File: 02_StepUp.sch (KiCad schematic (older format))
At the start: 31 parts, among them J301 Conn_02x04_Odd_Even, J302 Conn_02x04_Odd_Even, Q201 VS6412AE, U202 StepUp, U203 TPS40210

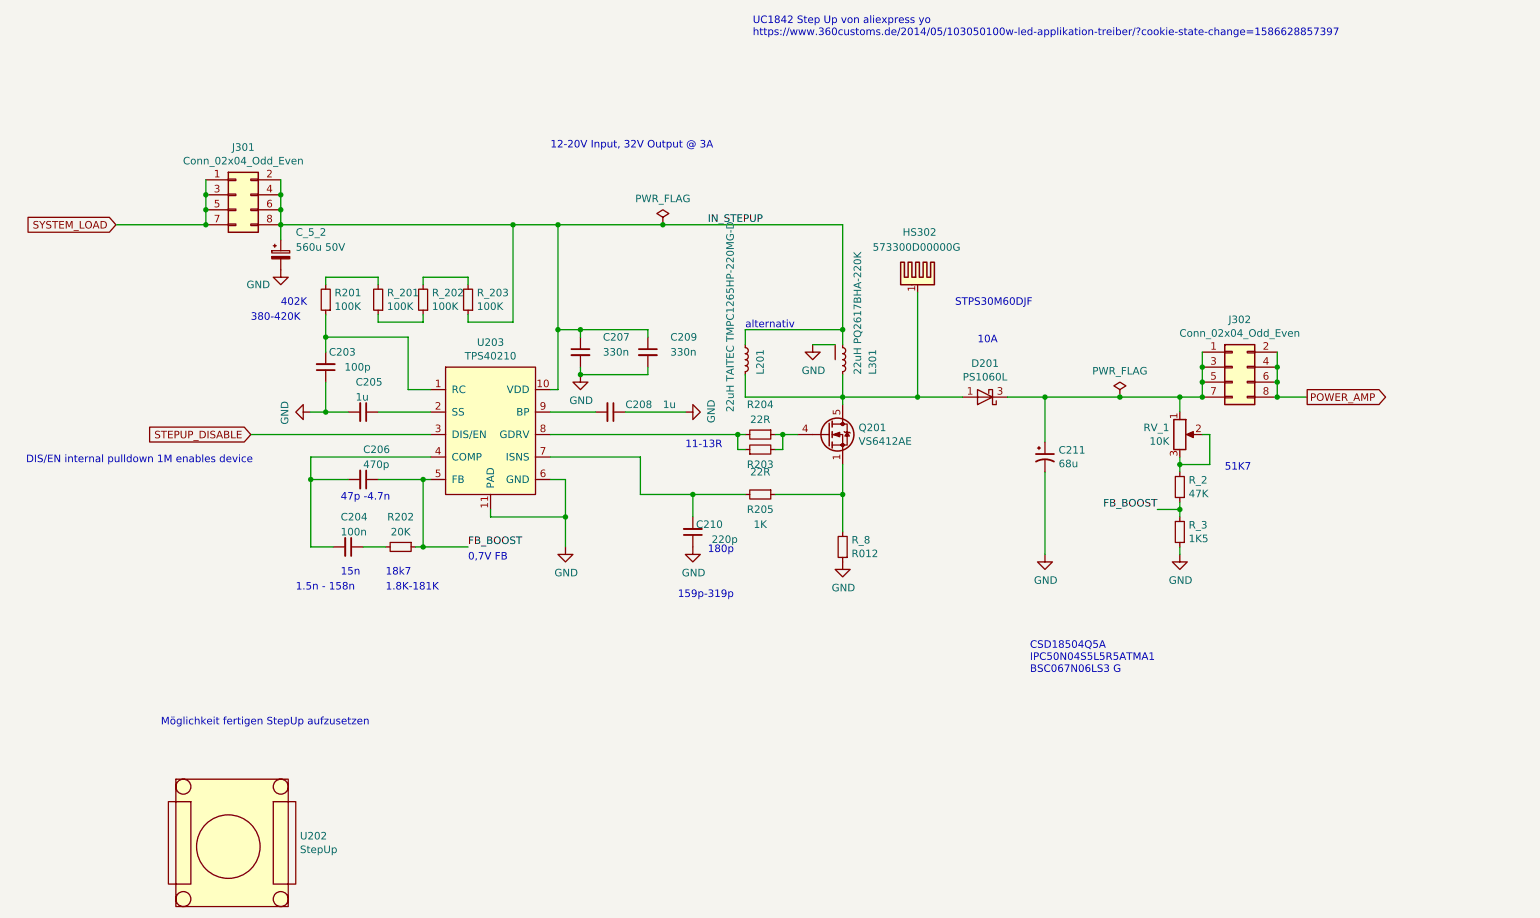
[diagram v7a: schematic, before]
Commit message: Platine in X um 25mm verkürzt
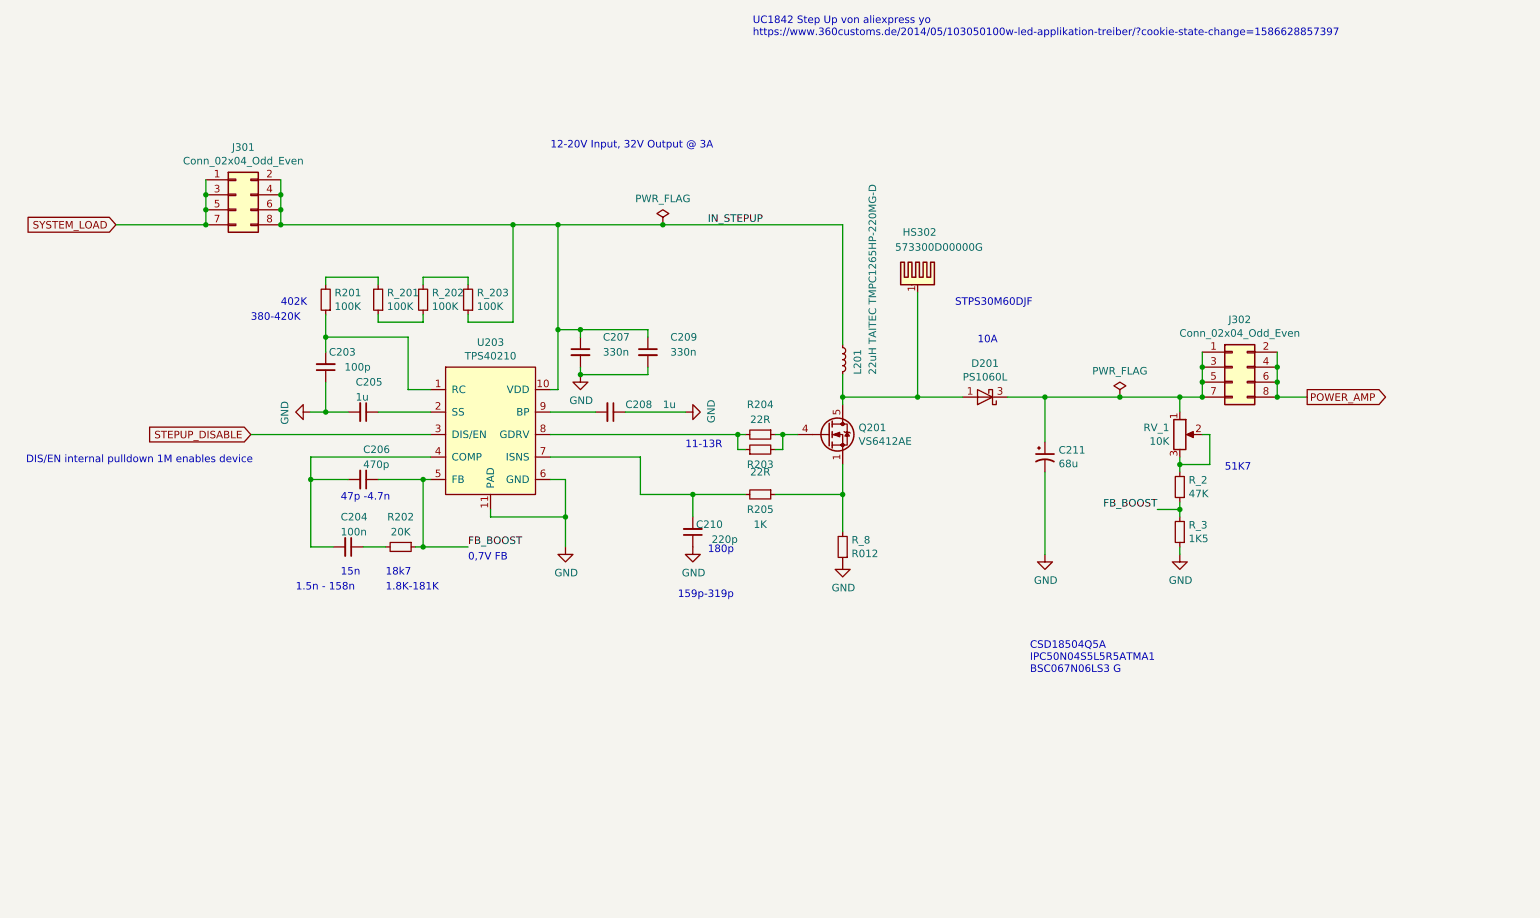
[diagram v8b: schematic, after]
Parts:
- removed C_5_2: 560u 50V, Capacitor_THT:CP_Radial_D12.5mm_P5.00mm, symbol Device:CP_Small
- removed L301: 22uH PQ2617BHA-220K, Inductor_SMD:PQ2617BHA-330K, symbol MukkeBox-rescue:L_Small_3-Device-MukkeBox-rescue
- removed U202: StepUp, Module:StepUpModul, symbol MukkeBox-rescue:StepUp-MySymbols-MukkeBox-rescue
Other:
- note removed: "Möglichkeit fertigen StepUp aufzusetzen"
- note removed: "alternativ"
- moved on the sheet: L201
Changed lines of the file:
@@
 Text GLabel 1850 2400 0    50   Input ~ 0
 SYSTEM_LOAD
-Wire Wire Line
-	2950 2500 2950 2400
 Text GLabel 9800 3550 2    50   Output ~ 0
 POWER_AMP
@@
 P 7200 2750
 F 0 "HS302" H 7100 3050 50  0000 L CNN
-F 1 "573300D00000G" H 6900 2950 50  0000 L CNN
+F 1 "573300D00000G" H 7050 2950 50  0000 L CNN
 F 2 "Heatsink:Heatsink_AAVID_573300D00010G_TO-263" H 7212 2700 50  0001 C CNN
 F 3 "https://www.mouser.de/datasheet/2/2/Aavid-Board-Level-Heatsinks-Catalog-2018-1507171.pdf" H 7212 2700 50  0001 C CNN
@@
 Wire Wire Line
 	8950 4000 8950 3950
-$Comp
-L Device:CP_Small C?
-U 1 1 5E9CBBA9
-P 2950 2600
-AR Path="/5E751A81/5E9CBBA9" Ref="C?"  Part="1"
-AR Path="/5E73BAE8/5E9CBBA9" Ref="C_5_2"  Part="1"
-F 0 "C_5_2" H 3050 2750 50  0000 L CNN
-F 1 "560u 50V" H 3050 2650 50  0000 L CNN
-F 2 "Capacitor_THT:CP_Radial_D12.5mm_P5.00mm" H 2950 2600 50  0001 C CNN
-F 3 "https://www.mouser.de/datasheet/2/420/United-Chemi-Con-1109128.pdf" H 2950 2600 50  0001 C CNN
-	1    2950 2600
-	1    0    0    -1
-$EndComp
 Wire Wire Line
 	2450 2400 1850 2400
@@
 	1    0    0    -1
 $EndComp
-$Comp
-L power:GND #PWR?
-U 1 1 5F07DA47
-P 2950 2700
-AR Path="/5EA6895E/5F07DA47" Ref="#PWR?"  Part="1"
-AR Path="/5E73BAE8/5F07DA47" Ref="#PWR0207"  Part="1"
-F 0 "#PWR0207" H 2950 2450 50  0001 C CNN
-F 1 "GND" H 2800 2600 50  0000 C CNN
-F 2 "" H 2950 2700 50  0001 C CNN
-F 3 "" H 2950 2700 50  0001 C CNN
-	1    2950 2700
-	1    0    0    -1
-$EndComp
 Connection ~ 8950 3550
 Wire Wire Line
@@
 Wire Wire Line
 	8950 4300 8950 4350
-$Comp
-L MukkeBox-rescue:StepUp-MySymbols-MukkeBox-rescue U202
-U 1 1 5FE6AEE3
-P 2600 6450
-F 0 "U202" H 3078 6421 50  0000 L CNN
-F 1 "StepUp" H 3078 6330 50  0000 L CNN
-F 2 "Module:StepUpModul" H 2600 6450 50  0001 C CNN
-F 3 "" H 2600 6450 50  0001 C CNN
-	1    2600 6450
-	1    0    0    -1
-$EndComp
-Text Notes 2150 5750 0    50   ~ 0
-Möglichkeit fertigen StepUp aufzusetzen
 $Comp
 L MukkeBox-rescue:TPS40210-MySymbols-MukkeBox-rescue U203
@@
 Wire Wire Line
 	5500 2400 6700 2400
-Wire Wire Line
-	6700 2400 6700 3100
 Wire Wire Line
 	4750 3500 4800 3500
@@
 	6300 3800 6400 3800
 $Comp
-L MukkeBox-rescue:L_Small_3-Device-MukkeBox-rescue L301
-U 1 1 5EDD1CAF
-P 6700 3300
-AR Path="/5EDD1CAF" Ref="L301"  Part="1"
-AR Path="/5E73BAE8/5EDD1CAF" Ref="L301"  Part="1"
-F 0 "L301" V 6900 3200 50  0000 L CNN
-F 1 "22uH PQ2617BHA-220K" V 6800 3200 50  0000 L CNN
-F 2 "Inductor_SMD:PQ2617BHA-330K" H 6700 3300 50  0001 C CNN
-F 3 "https://www.mouser.de/datasheet/2/54/bourns_PQ2617BHA_datasheet-1159314.pdf" H 6700 3300 50  0001 C CNN
-	1    6700 3300
-	1    0    0    -1
-$EndComp
-$Comp
-L power:GND #PWR0201
-U 1 1 5EDD85E2
-P 6500 3200
-F 0 "#PWR0201" H 6500 2950 50  0001 C CNN
-F 1 "GND" H 6505 3027 50  0000 C CNN
-F 2 "" H 6500 3200 50  0001 C CNN
-F 3 "" H 6500 3200 50  0001 C CNN
-	1    6500 3200
-	1    0    0    -1
-$EndComp
-Wire Wire Line
-	6650 3200 6500 3200
-$Comp
 L Device:L_Small L201
 U 1 1 5EFA9CC8
-P 6050 3300
-F 0 "L201" V 6150 3200 50  0000 L CNN
-F 1 "22uH TAITEC TMPC1265HP-220MG-D " V 5950 2950 50  0000 L CNN
-F 2 "Inductor_SMD:TAITEC TMPC1265HP-220MG-D" H 6050 3300 50  0001 C CNN
-F 3 "https://datasheet.lcsc.com/szlcsc/TAITEC-TMPC1265HP-220MG-D_C305224.pdf" H 6050 3300 50  0001 C CNN
-	1    6050 3300
-	1    0    0    -1
-$EndComp
-Wire Wire Line
-	6050 3200 6050 3100
-Wire Wire Line
-	6050 3100 6700 3100
-Connection ~ 6700 3100
-Wire Wire Line
-	6700 3100 6700 3200
-Wire Wire Line
-	6050 3400 6050 3550
-Wire Wire Line
-	6050 3550 6700 3550
-Text Notes 6050 3100 0    50   ~ 0
-alternativ
+P 6700 3300
+F 0 "L201" V 6800 3200 50  0000 L CNN
+F 1 "22uH TAITEC TMPC1265HP-220MG-D " V 6900 3200 50  0000 L CNN
+F 2 "Inductor_SMD:TAITEC TMPC1265HP-220MG-D" H 6700 3300 50  0001 C CNN
+F 3 "https://datasheet.lcsc.com/szlcsc/TAITEC-TMPC1265HP-220MG-D_C305224.pdf" H 6700 3300 50  0001 C CNN
+	1    6700 3300
+	1    0    0    -1
+$EndComp
 Text Notes 4200 4650 0    50   ~ 0
 0,7V FB
@@
 Wire Wire Line
 	3950 3800 2750 3800
+Wire Wire Line
+	6700 2400 6700 3200
 $EndSCHEMATC
